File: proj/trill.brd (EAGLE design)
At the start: 44.2 x 108.7 mm, 127 parts, among them J1 SPKRAST_01532MR, J2 MICCMA-4544PF-W, J3 ADAFRUIT_OLED_13, J4 DM3D-SFDM, J5 SJ1-3523N, J6 CONUFL001, M1 Z3OC_VIB_MOTOR, U1 SIM5300EA, U10 3.3V 600mA, U11 MCP1642B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

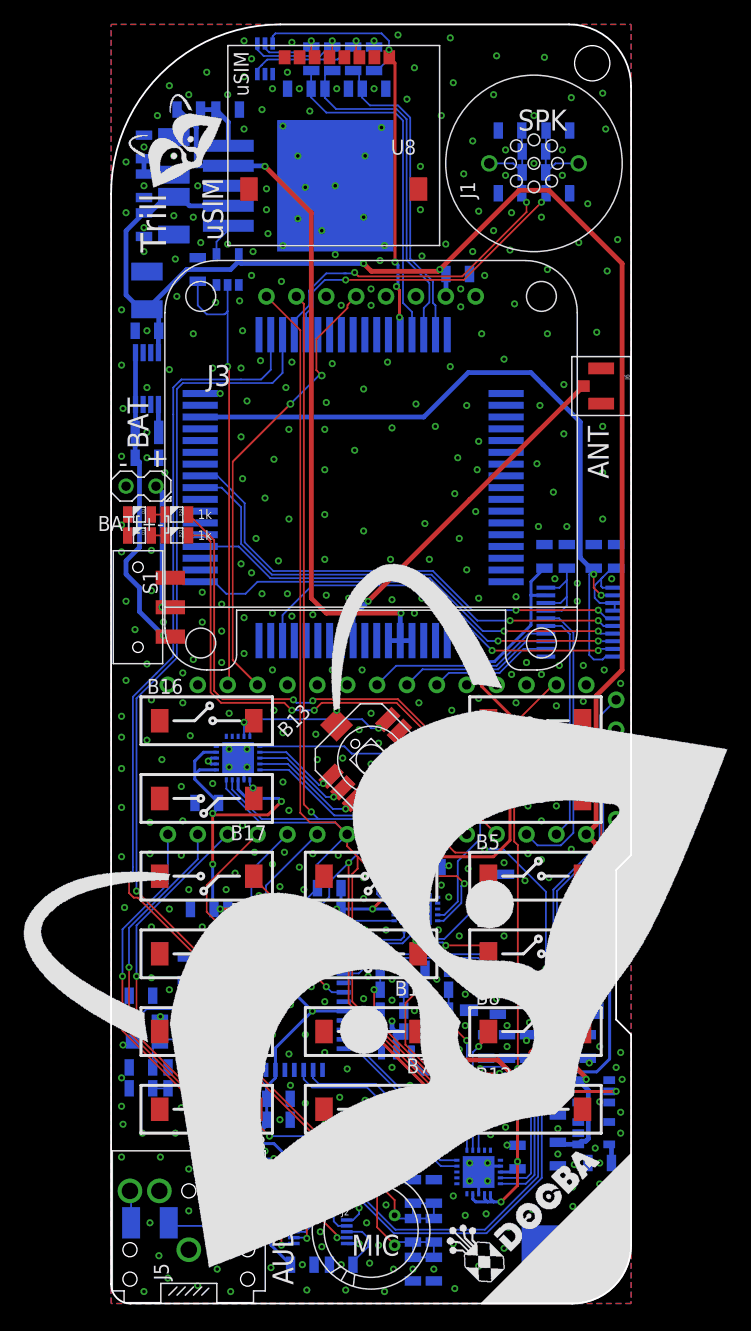
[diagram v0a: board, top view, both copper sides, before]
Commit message: Fixed Trill board (Jack connector & GSM_PWR_KEY)
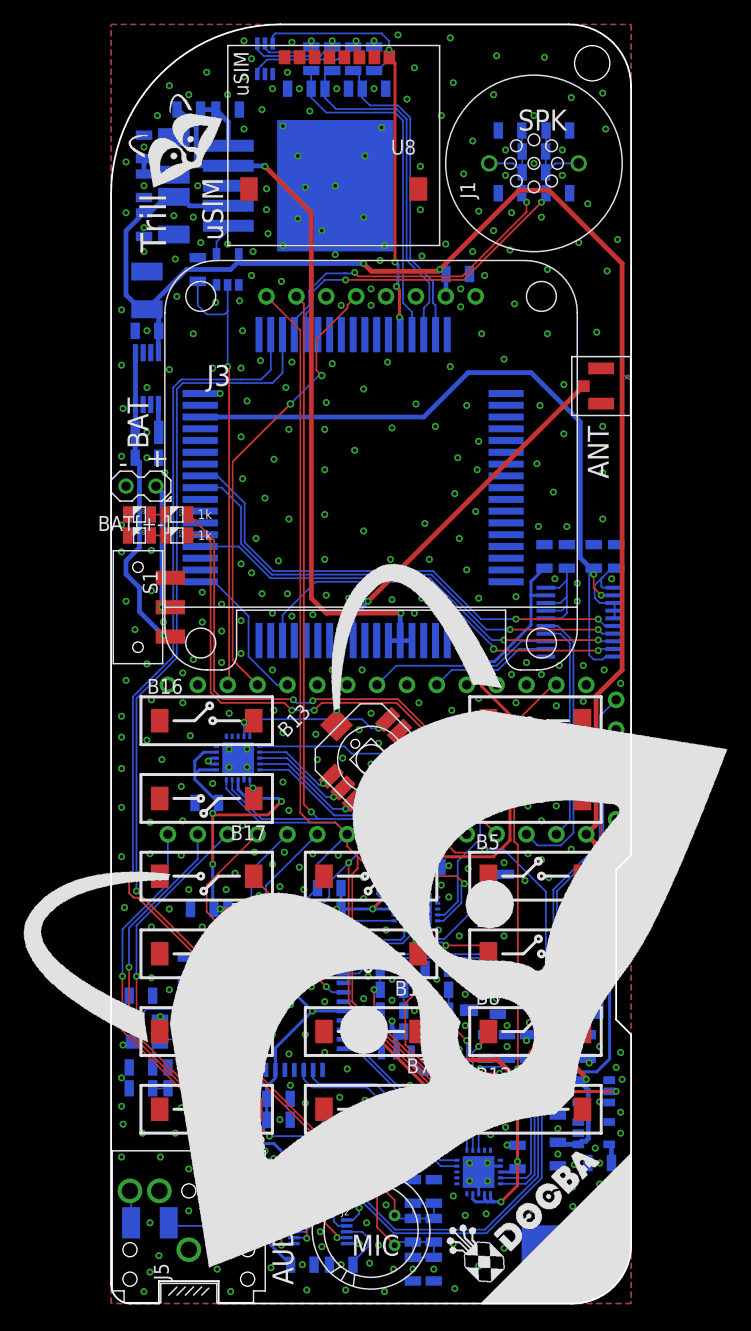
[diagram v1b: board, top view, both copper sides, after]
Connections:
- removed net N$24: U1.P$1, U6.P$8
- net GSM_PWR_KEY: now also N1.5, U1.P$1; no longer N1.9, U6.P$13
- net GSM_RING: now also U6.P$13; no longer U6.P$14
- net GSM_RXD: now also U6.P$15; no longer U6.P$16
- net GSM_TXD: now also U6.P$14; no longer U6.P$15
- net N$25: now also U6.P$8; no longer U6.P$7
- net N$26: now also U6.P$7; no longer U6.P$6
- net N$27: now also U6.P$6; no longer U6.P$5
- net N$30: now also U6.P$16
- net N$32: now also U6.P$5
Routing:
- net N$24: track 38.2 -> 0.00 mm, vias 2 -> 0
- net N$30: track 9.19 -> 11.8 mm
- net GSM_TXD: track 19.8 -> 19.1 mm
- net GSM_RXD: track 24.7 -> 24.0 mm
- net N$32: track 8.19 -> 8.84 mm
- net GND: vias 492 -> 491
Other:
- outline, holes or cut-outs redrawn
